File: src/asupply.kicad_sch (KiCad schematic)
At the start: 124 parts, among them U10 LT3081xDF, U11 LT3042xMSE, U12 LT3045xMSE, U13 LT3045xMSE, U14 LT3042xMSE, U15 LT3094xMSE, U16 LTC3261, U17 LT3042xMSE

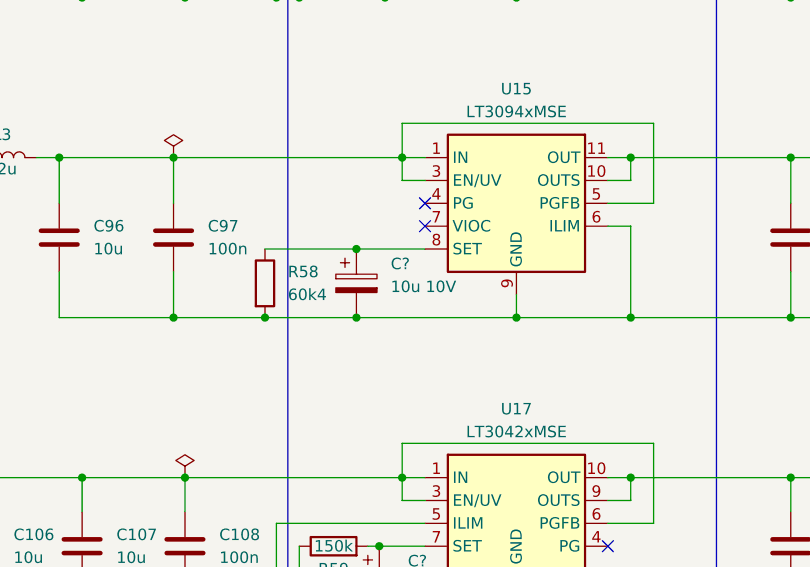
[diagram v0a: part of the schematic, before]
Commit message: sch, pcb: correct polarity of LT3094xMSE C_Set
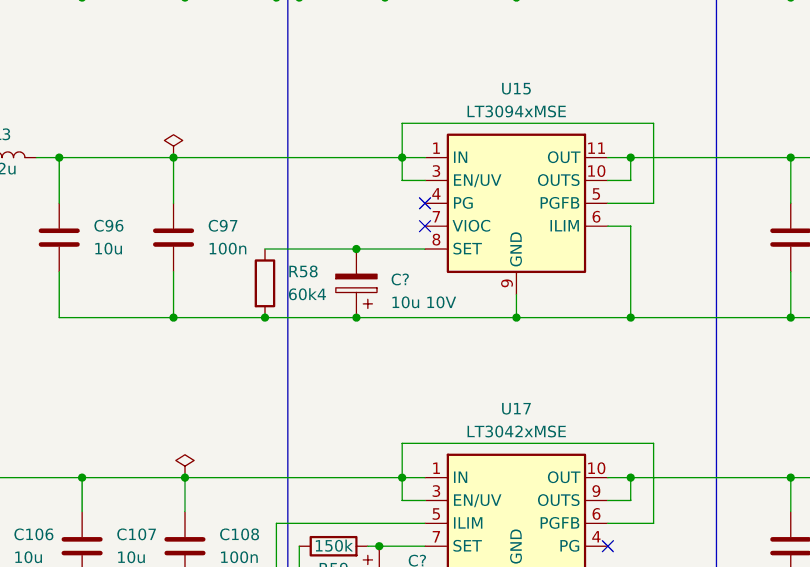
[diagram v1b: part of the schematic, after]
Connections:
- net GND: now also C?.1; no longer C?.2
- net at R58.1, U15.8 (SET): now also C?.2; no longer C?.1
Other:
- moved on the sheet: C?
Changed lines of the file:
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@@
   (junction (at 199.39 252.73) (diameter 0) (color 0 0 0 0)
   )
+  (junction (at 205.74 212.09) (diameter 0) (color 0 0 0 0)
+  )
   (junction (at 65.405 52.07) (diameter 0) (color 0 0 0 0)
   )
@@
   (junction (at 160.02 201.93) (diameter 0) (color 0 0 0 0)
   )
+  (junction (at 195.58 219.71) (diameter 0) (color 0 0 0 0)
+  )
   (junction (at 186.69 138.43) (diameter 0) (color 0 0 0 0)
   )
@@
   (junction (at 101.6 201.93) (diameter 0) (color 0 0 0 0)
   )
-  (junction (at 205.74 219.71) (diameter 0) (color 0 0 0 0)
-  )
   (junction (at 208.915 184.15) (diameter 0) (color 0 0 0 0)
   )
@@
   (junction (at 254 201.93) (diameter 0) (color 0 0 0 0)
   )
+  (junction (at 205.74 219.71) (diameter 0) (color 0 0 0 0)
+  )
   (junction (at 85.09 176.53) (diameter 0) (color 0 0 0 0)
   )
@@
   (junction (at 175.26 153.67) (diameter 0) (color 0 0 0 0)
   )
-  (junction (at 205.74 212.09) (diameter 0) (color 0 0 0 0)
-  )
   (junction (at 73.66 201.93) (diameter 0) (color 0 0 0 0)
   )
@@
   (junction (at 42.545 52.07) (diameter 0) (color 0 0 0 0)
   )
-  (junction (at 195.58 219.71) (diameter 0) (color 0 0 0 0)
-  )
   (junction (at 236.22 237.49) (diameter 0) (color 0 0 0 0)
   )
   (junction (at 281.94 153.67) (diameter 0) (color 0 0 0 0)
   )
-  (junction (at 223.52 219.71) (diameter 0) (color 0 0 0 0)
-  )
   (junction (at 175.26 76.2) (diameter 0) (color 0 0 0 0)
   )
@@
   (junction (at 163.83 44.45) (diameter 0) (color 0 0 0 0)
   )
+  (junction (at 223.52 219.71) (diameter 0) (color 0 0 0 0)
+  )
   (junction (at 199.39 184.15) (diameter 0) (color 0 0 0 0)
   )
@@
     (stroke (width 0) (type default))
   )
+  (wire (pts (xy 195.58 219.71) (xy 205.74 219.71))
+    (stroke (width 0) (type default))
+  )
   (wire (pts (xy 186.69 44.45) (xy 214.63 44.45))
     (stroke (width 0) (type default))
@@
     (stroke (width 0) (type default))
   )
-  (wire (pts (xy 205.74 212.09) (xy 213.36 212.09))
-    (stroke (width 0) (type default))
-  )
   (wire (pts (xy 210.82 78.74) (xy 210.82 76.2))
     (stroke (width 0) (type default))
@@
     (stroke (width 0) (type default))
   )
-  (wire (pts (xy 195.58 219.71) (xy 205.74 219.71))
-    (stroke (width 0) (type default))
-  )
   (wire (pts (xy 73.66 237.49) (xy 88.9 237.49))
     (stroke (width 0) (type default))
@@
     (stroke (width 0) (type default))
   )
+  (wire (pts (xy 195.58 212.09) (xy 205.74 212.09))
+    (stroke (width 0) (type default))
+  )
   (wire (pts (xy 267.97 252.73) (xy 267.97 248.92))
     (stroke (width 0) (type default))
@@
     (stroke (width 0) (type default))
   )
-  (wire (pts (xy 205.74 219.71) (xy 223.52 219.71))
-    (stroke (width 0) (type default))
-  )
   (wire (pts (xy 196.85 242.57) (xy 196.85 252.73))
     (stroke (width 0) (type default))
@@
     (stroke (width 0) (type default))
   )
+  (wire (pts (xy 205.74 212.09) (xy 213.36 212.09))
+    (stroke (width 0) (type default))
+  )
   (wire (pts (xy 281.94 138.43) (xy 281.94 142.24))
     (stroke (width 0) (type default))
@@
     (stroke (width 0) (type default))
   )
+  (wire (pts (xy 205.74 219.71) (xy 223.52 219.71))
+    (stroke (width 0) (type default))
+  )
   (wire (pts (xy 199.39 83.82) (xy 199.39 91.44))
     (stroke (width 0) (type default))
@@
     (stroke (width 0) (type default))
   )
-  (wire (pts (xy 195.58 212.09) (xy 205.74 212.09))
-    (stroke (width 0) (type default))
-  )
   (wire (pts (xy 53.975 44.45) (xy 65.405 44.45))
     (stroke (width 0) (type default))
@@
     )
   )
-  (symbol (lib_id "Device:C_Polarized") (at 205.74 215.9 0) (unit 1)
+  (symbol (lib_id "Device:C_Polarized") (at 205.74 215.9 180) (unit 1)
     (in_bom yes) (on_board yes) (dnp no) (fields_autoplaced)
-    (property "Reference" "C?" (at 209.55 213.741 0)
-      (effects (font (size 1.27 1.27)) (justify left))
+    (property "Reference" "C?" (at 209.55 215.519 0)
+      (effects (font (size 1.27 1.27)) (justify right))
     )
-    (property "Value" "10u 10V" (at 209.55 216.281 0)
-      (effects (font (size 1.27 1.27)) (justify left))
+    (property "Value" "10u 10V" (at 209.55 218.059 0)
+      (effects (font (size 1.27 1.27)) (justify right))
     )
-    (property "Footprint" "Capacitor_Tantalum_SMD:CP_EIA-3528-21_Kemet-B" (at 206.7052 219.71 0)
+    (property "Footprint" "Capacitor_Tantalum_SMD:CP_EIA-3528-21_Kemet-B" (at 204.7748 212.09 0)
       (effects (font (size 1.27 1.27)) hide)
     )
